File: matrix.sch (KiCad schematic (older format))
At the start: 134 parts, among them SW1 SW_Push, SW10 SW_Push, SW11 SW_Push, SW12 SW_Push, SW13 SW_Push, SW14 SW_Push, SW15 SW_Push, SW16 SW_Push, SW17 SW_Push, SW18 SW_Push, SW19 SW_Push, SW2 SW_Push, SW20 SW_Push, SW21 SW_Push, SW22 SW_Push, SW23 SW_Push, SW24 SW_Push, SW25 SW_Push, SW26 SW_Push, SW27 SW_Push, SW28 SW_Push, SW29 SW_Push, SW3 SW_Push, SW30 SW_Push, SW31 SW_Push, SW32 SW_Push, SW33 SW_Push, SW34 SW_Push, SW35 SW_Push, SW36 SW_Push, SW37 SW_Push, SW38 SW_Push, SW39 SW_Push, SW4 SW_Push, SW40 SW_Push, SW41 SW_Push, SW42 SW_Push, SW43 SW_Push, SW44 SW_Push, SW45 SW_Push, SW46 SW_Push, SW47 SW_Push, SW48 SW_Push, SW49 SW_Push, SW5 SW_Push, SW50 SW_Push, SW51 SW_Push, SW52 SW_Push, SW53 SW_Push, SW54 SW_Push, SW55 SW_Push, SW56 SW_Push, SW57 SW_Push, SW58 SW_Push, SW59 SW_Push, SW6 SW_Push, SW60 SW_Push, SW61 SW_Push, SW62 SW_Push, SW63 SW_Push, SW64 SW_Push, SW65 SW_Push, SW66 SW_Push, SW67 SW_Push, SW7 SW_Push, SW8 SW_Push, SW9 SW_Push

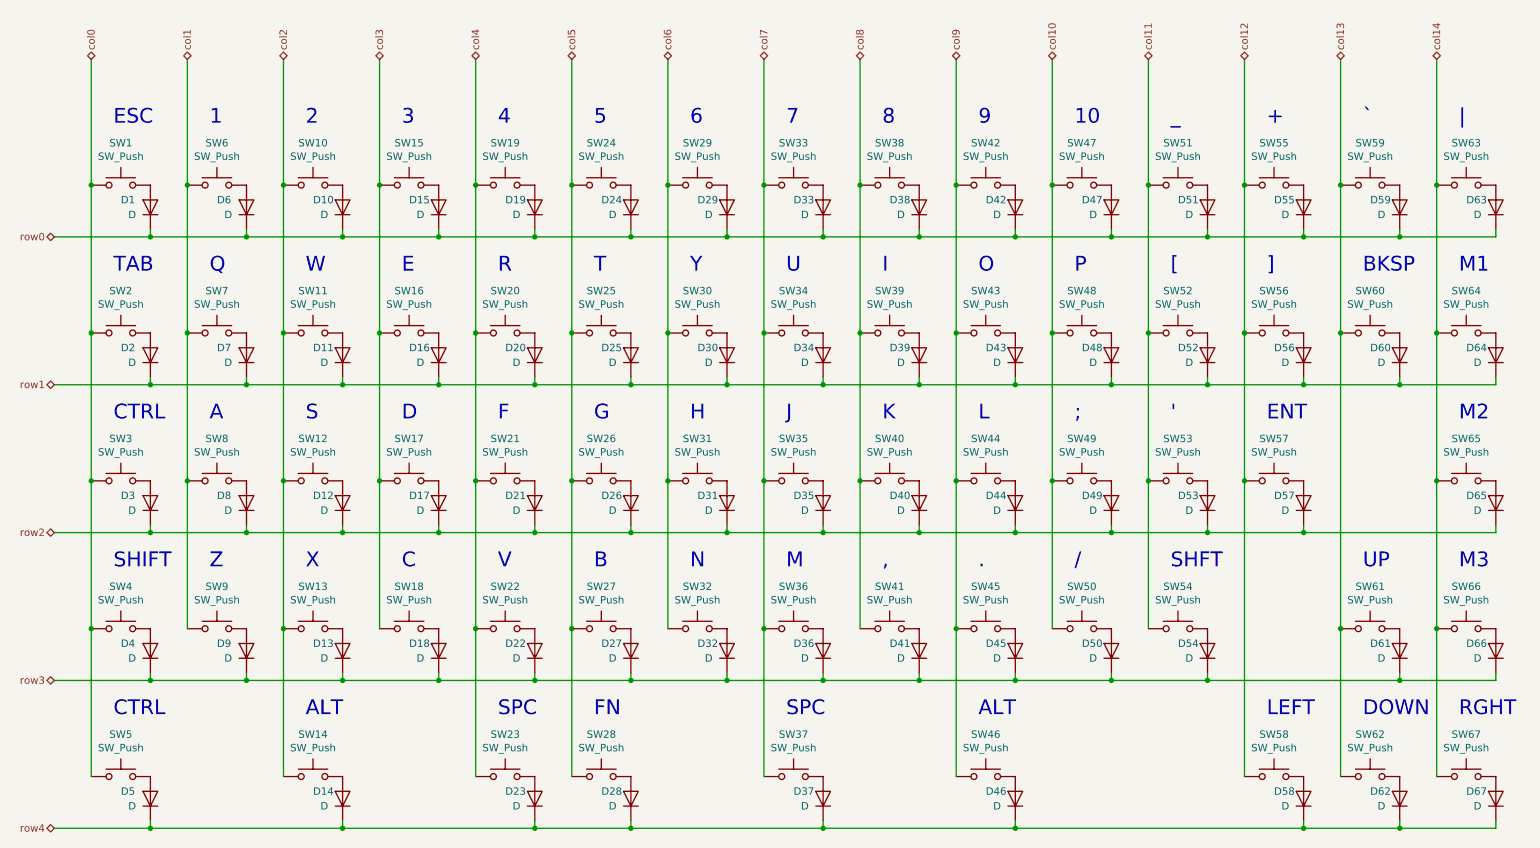
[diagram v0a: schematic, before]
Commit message: Remove top row and decrease all other row indexes by 1 to adjust.
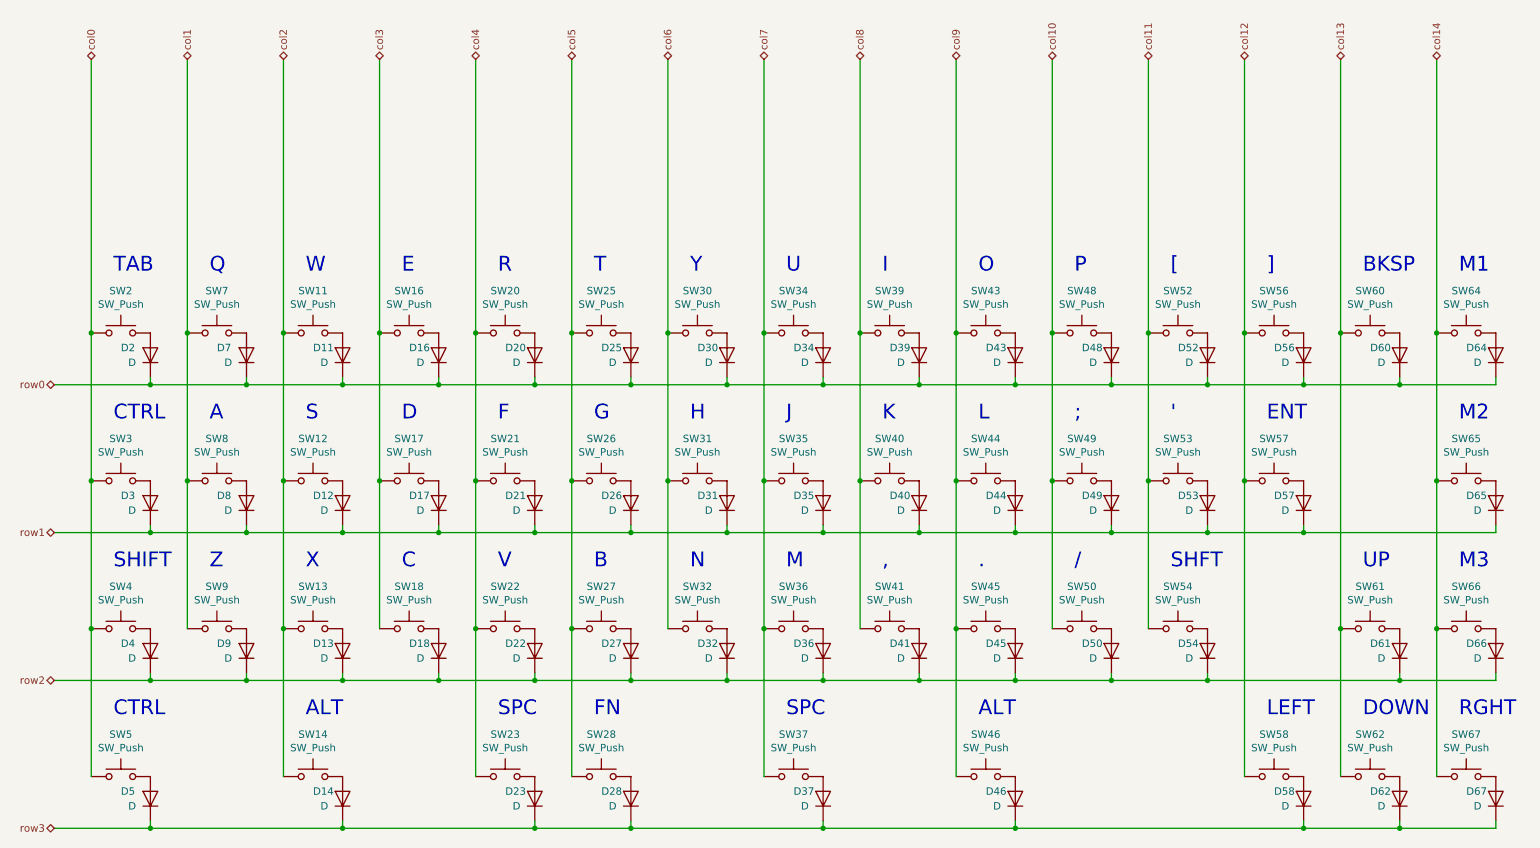
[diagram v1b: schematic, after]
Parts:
- removed D1, D10, D15, D19, D24, D29, D33, D38, D42, D47, D51, D55, D59, D6, D63: D, Diodes_SMD:D_SOD-123, symbol Device:D
- removed SW1, SW10, SW15, SW19, SW24, SW29, SW33, SW38, SW42, SW47, SW51, SW55, SW59, SW6, SW63: SW_Push, Fate_Parts:SW_Cherry_MX_1.00u_PCB, symbol Switch:SW_Push
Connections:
- net row4 is gone; now on net row3: D14.1 (K), D23.1 (K), D28.1 (K), D37.1 (K), D46.1 (K), D5.1 (K), D58.1 (K), D62.1 (K), D67.1 (K)
- net row0: now also D11.1 (K), D16.1 (K), D2.1 (K), D20.1 (K), D25.1 (K), D30.1 (K), D34.1 (K), D39.1 (K), D43.1 (K), D48.1 (K), D52.1 (K), D56.1 (K), D60.1 (K), D64.1 (K), D7.1 (K)
- net row1: now also D12.1 (K), D17.1 (K), D21.1 (K), D26.1 (K), D3.1 (K), D31.1 (K), D35.1 (K), D40.1 (K), D44.1 (K), D49.1 (K), D53.1 (K), D57.1 (K), D65.1 (K), D8.1 (K); no longer D11.1 (K), D16.1 (K), D2.1 (K), D20.1 (K), D25.1 (K), D30.1 (K), D34.1 (K), D39.1 (K), D43.1 (K), D48.1 (K), D52.1 (K), D56.1 (K), D60.1 (K), D64.1 (K), D7.1 (K)
- net row2: now also D13.1 (K), D18.1 (K), D22.1 (K), D27.1 (K), D32.1 (K), D36.1 (K), D4.1 (K), D41.1 (K), D45.1 (K), D50.1 (K), D54.1 (K), D61.1 (K), D66.1 (K), D9.1 (K); no longer D12.1 (K), D17.1 (K), D21.1 (K), D26.1 (K), D3.1 (K), D31.1 (K), D35.1 (K), D40.1 (K), D44.1 (K), D49.1 (K), D53.1 (K), D57.1 (K), D65.1 (K), D8.1 (K)
- net row3: no longer D13.1 (K), D18.1 (K), D22.1 (K), D27.1 (K), D32.1 (K), D36.1 (K), D4.1 (K), D41.1 (K), D45.1 (K), D50.1 (K), D54.1 (K), D61.1 (K), D66.1 (K), D9.1 (K)
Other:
- note removed: "+"
- note removed: "1"
- note removed: "10"
- note removed: "2"
- note removed: "3"
- note removed: "4"
- note removed: "5"
- note removed: "6"
- note removed: "7"
- note removed: "8"
- note removed: "9"
- note removed: "ESC"
- note removed: "_"
- note removed: "`"
- note removed: "|"

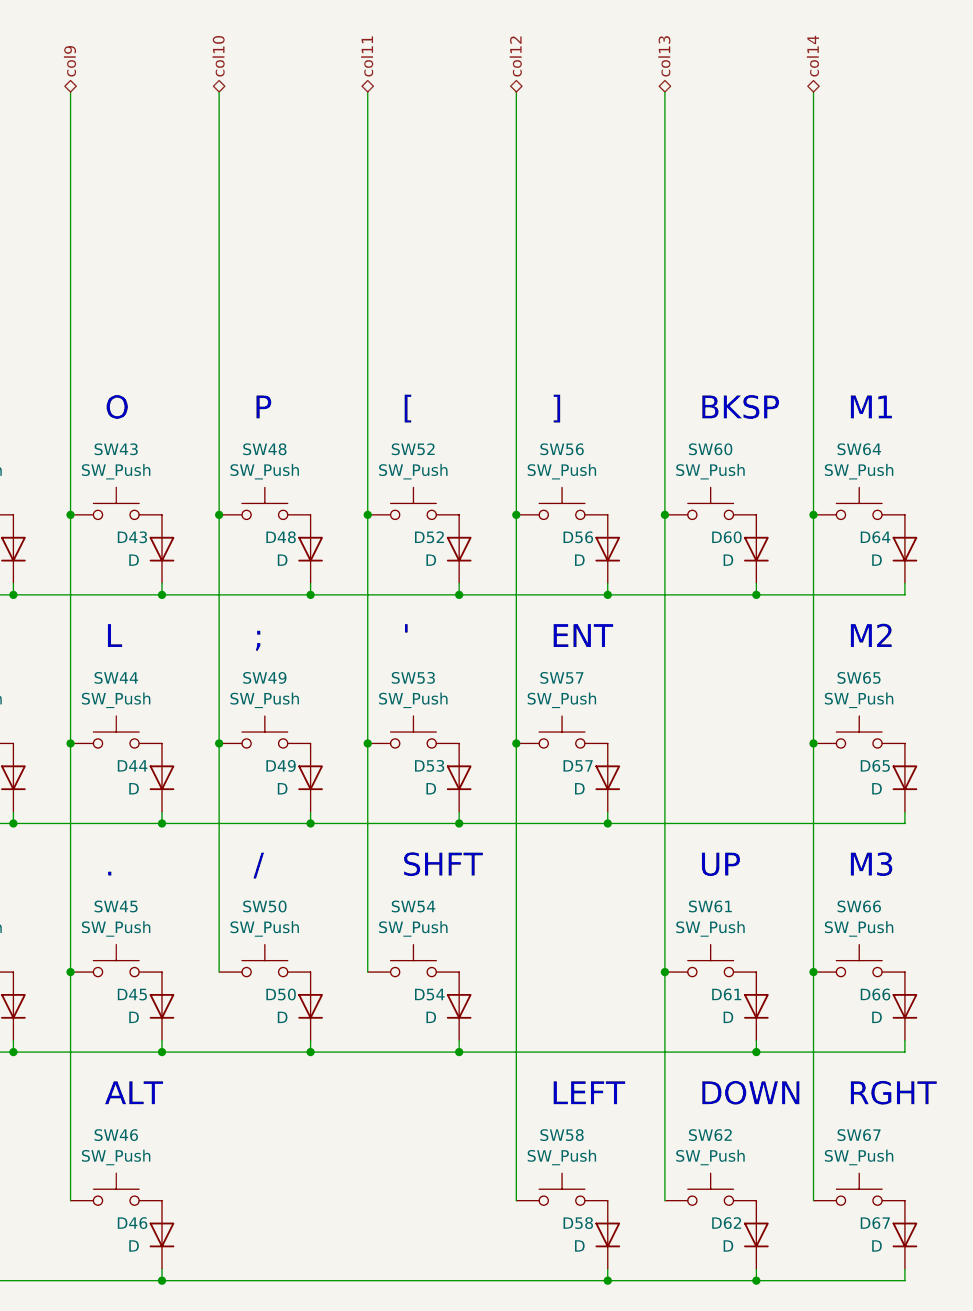
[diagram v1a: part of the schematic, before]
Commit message: Redesign alpha layout for natural finger spread.
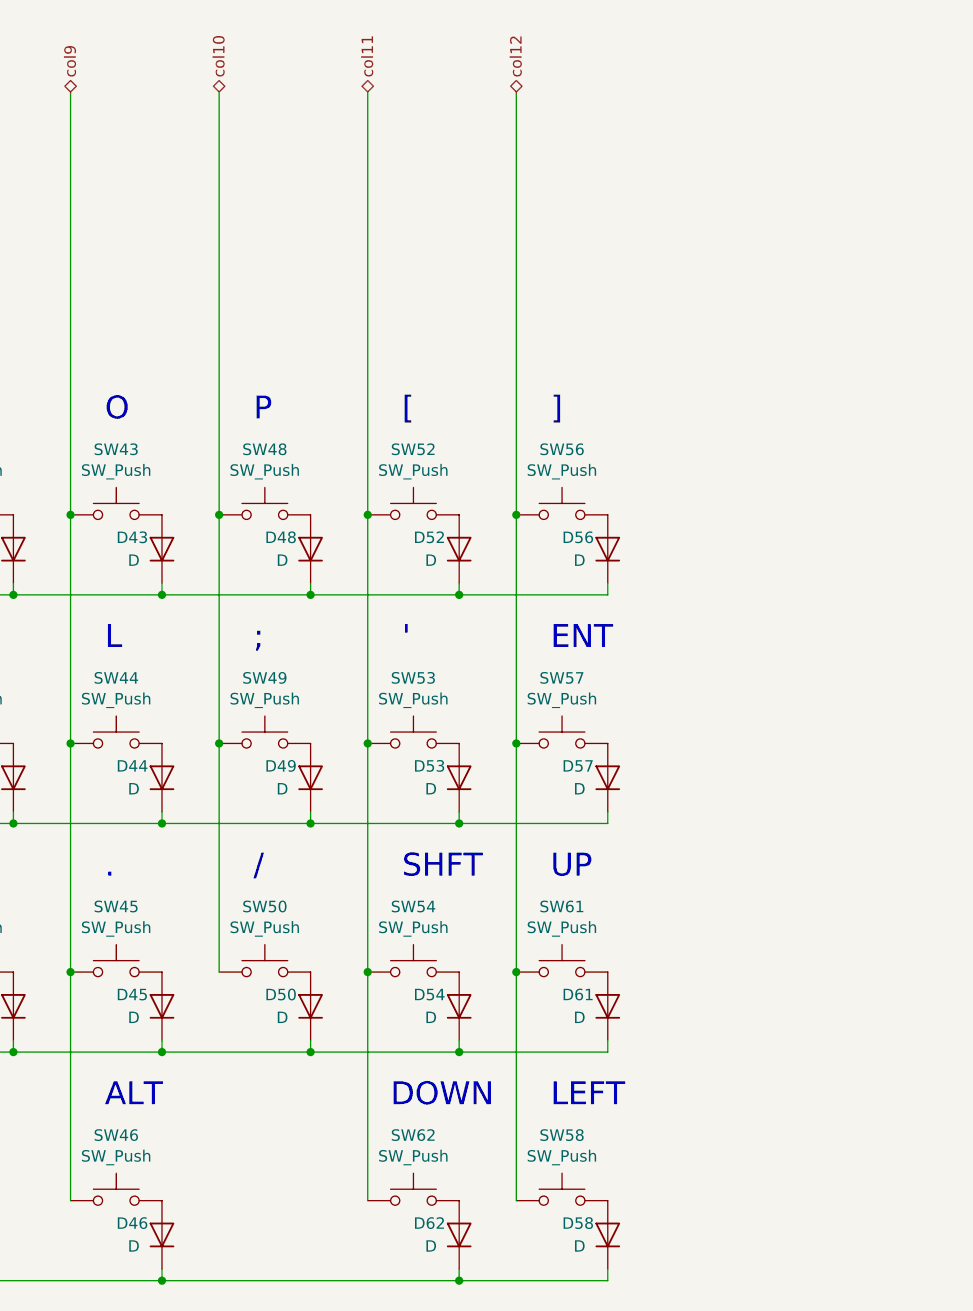
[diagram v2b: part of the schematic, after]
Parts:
- removed D60, D64, D65, D66, D67: D, Diodes_SMD:D_SOD-123, symbol Device:D
- removed SW60: SW_Push, Fate_Parts:SW_Cherry_MX_1.50u_PCB, symbol Switch:SW_Push
- removed SW64, SW65, SW66, SW67: SW_Push, Fate_Parts:SW_Cherry_MX_1.00u_PCB, symbol Switch:SW_Push
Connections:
- net col11: now also SW62.1
- net col12: now also SW61.1
- removed net col13: SW61.1, SW62.1
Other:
- note removed: "BKSP"
- note removed: "M1"
- note removed: "M2"
- note removed: "M3"
- note removed: "RGHT\n"
- moved on the sheet: D61, D62, SW61, SW62
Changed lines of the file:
@@
 Text HLabel 9000 750  1    50   3State ~ 0
 col12
-Text HLabel 9650 750  1    50   3State ~ 0
-col13
-Text HLabel 10300 750  1    50   3State ~ 0
-col14
 Wire Wire Line
 	950  2950 1600 2950
@@
 Connection ~ 9000 2600
 $Comp
-L Switch:SW_Push SW60
-U 1 1 5C6656F5
-P 9850 2600
-F 0 "SW60" H 9850 2885 50  0000 C CNN
-F 1 "SW_Push" H 9850 2794 50  0000 C CNN
-F 2 "Fate_Parts:SW_Cherry_MX_1.50u_PCB" H 9850 2800 50  0001 C CNN
-F 3 "" H 9850 2800 50  0001 C CNN
-	1    9850 2600
-	1    0    0    -1
-$EndComp
-$Comp
-L Device:D D60
-U 1 1 5C6656FC
-P 10050 2750
-F 0 "D60" V 10100 2950 50  0000 R CNN
-F 1 "D" V 10000 2900 50  0000 R CNN
-F 2 "Diodes_SMD:D_SOD-123" H 10050 2750 50  0001 C CNN
-F 3 "~" H 10050 2750 50  0001 C CNN
-	1    10050 2750
-	0    -1   -1   0
-$EndComp
-Wire Wire Line
-	10050 2900 10050 2950
-$Comp
 L Switch:SW_Push SW61
 U 1 1 5C66570E
-P 9850 4600
-F 0 "SW61" H 9850 4885 50  0000 C CNN
-F 1 "SW_Push" H 9850 4794 50  0000 C CNN
-F 2 "Fate_Parts:SW_Cherry_MX_1.00u_PCB" H 9850 4800 50  0001 C CNN
-F 3 "" H 9850 4800 50  0001 C CNN
-	1    9850 4600
-	1    0    0    -1
-$EndComp
-Wire Wire Line
-	9650 4600 9650 5600
+P 9200 4600
+F 0 "SW61" H 9200 4885 50  0000 C CNN
+F 1 "SW_Push" H 9200 4794 50  0000 C CNN
+F 2 "Fate_Parts:SW_Cherry_MX_1.00u_PCB" H 9200 4800 50  0001 C CNN
+F 3 "" H 9200 4800 50  0001 C CNN
+	1    9200 4600
+	1    0    0    -1
+$EndComp
 $Comp
 L Switch:SW_Push SW62
 U 1 1 5C665716
-P 9850 5600
-F 0 "SW62" H 9850 5885 50  0000 C CNN
-F 1 "SW_Push" H 9850 5794 50  0000 C CNN
-F 2 "Fate_Parts:SW_Cherry_MX_1.00u_PCB" H 9850 5800 50  0001 C CNN
-F 3 "" H 9850 5800 50  0001 C CNN
-	1    9850 5600
+P 8550 5600
+F 0 "SW62" H 8550 5885 50  0000 C CNN
+F 1 "SW_Push" H 8550 5794 50  0000 C CNN
+F 2 "Fate_Parts:SW_Cherry_MX_1.00u_PCB" H 8550 5800 50  0001 C CNN
+F 3 "" H 8550 5800 50  0001 C CNN
+	1    8550 5600
 	1    0    0    -1
 $EndComp
@@
 L Device:D D61
 U 1 1 5C665724
-P 10050 4750
-F 0 "D61" V 10100 4950 50  0000 R CNN
-F 1 "D" V 10000 4900 50  0000 R CNN
-F 2 "Diodes_SMD:D_SOD-123" H 10050 4750 50  0001 C CNN
-F 3 "~" H 10050 4750 50  0001 C CNN
-	1    10050 4750
+P 9400 4750
+F 0 "D61" V 9450 4950 50  0000 R CNN
+F 1 "D" V 9350 4900 50  0000 R CNN
+F 2 "Diodes_SMD:D_SOD-123" H 9400 4750 50  0001 C CNN
+F 3 "~" H 9400 4750 50  0001 C CNN
+	1    9400 4750
 	0    -1   -1   0
 $EndComp
@@
 L Device:D D62
 U 1 1 5C66572B
-P 10050 5750
-F 0 "D62" V 10100 5950 50  0000 R CNN
-F 1 "D" V 10000 5900 50  0000 R CNN
-F 2 "Diodes_SMD:D_SOD-123" H 10050 5750 50  0001 C CNN
-F 3 "~" H 10050 5750 50  0001 C CNN
-	1    10050 5750
-	0    -1   -1   0
-$EndComp
-Wire Wire Line
-	10050 5900 10050 5950
-Wire Wire Line
-	10050 4900 10050 4950
-Connection ~ 9650 4600
-Connection ~ 9650 2600
-$Comp
-L Switch:SW_Push SW64
-U 1 1 5C66EC7D
-P 10500 2600
-F 0 "SW64" H 10500 2885 50  0000 C CNN
-F 1 "SW_Push" H 10500 2794 50  0000 C CNN
-F 2 "Fate_Parts:SW_Cherry_MX_1.00u_PCB" H 10500 2800 50  0001 C CNN
-F 3 "" H 10500 2800 50  0001 C CNN
-	1    10500 2600
-	1    0    0    -1
-$EndComp
-$Comp
-L Device:D D64
-U 1 1 5C66EC84
-P 10700 2750
-F 0 "D64" V 10750 2950 50  0000 R CNN
-F 1 "D" V 10650 2900 50  0000 R CNN
-F 2 "Diodes_SMD:D_SOD-123" H 10700 2750 50  0001 C CNN
-F 3 "~" H 10700 2750 50  0001 C CNN
-	1    10700 2750
-	0    -1   -1   0
-$EndComp
-Wire Wire Line
-	10700 2900 10700 2950
-$Comp
-L Switch:SW_Push SW65
-U 1 1 5C66EC8F
-P 10500 3600
-F 0 "SW65" H 10500 3885 50  0000 C CNN
-F 1 "SW_Push" H 10500 3794 50  0000 C CNN
-F 2 "Fate_Parts:SW_Cherry_MX_1.00u_PCB" H 10500 3800 50  0001 C CNN
-F 3 "" H 10500 3800 50  0001 C CNN
-	1    10500 3600
-	1    0    0    -1
-$EndComp
-$Comp
-L Switch:SW_Push SW66
-U 1 1 5C66EC96
-P 10500 4600
-F 0 "SW66" H 10500 4885 50  0000 C CNN
-F 1 "SW_Push" H 10500 4794 50  0000 C CNN
-F 2 "Fate_Parts:SW_Cherry_MX_1.00u_PCB" H 10500 4800 50  0001 C CNN
-F 3 "" H 10500 4800 50  0001 C CNN
-	1    10500 4600
-	1    0    0    -1
-$EndComp
-Wire Wire Line
-	10300 4600 10300 5600
-$Comp
-L Switch:SW_Push SW67
-U 1 1 5C66EC9E
-P 10500 5600
-F 0 "SW67" H 10500 5885 50  0000 C CNN
-F 1 "SW_Push" H 10500 5794 50  0000 C CNN
-F 2 "Fate_Parts:SW_Cherry_MX_1.00u_PCB" H 10500 5800 50  0001 C CNN
-F 3 "" H 10500 5800 50  0001 C CNN
-	1    10500 5600
-	1    0    0    -1
-$EndComp
-$Comp
-L Device:D D65
-U 1 1 5C66ECA5
-P 10700 3750
-F 0 "D65" V 10750 3950 50  0000 R CNN
-F 1 "D" V 10650 3900 50  0000 R CNN
-F 2 "Diodes_SMD:D_SOD-123" H 10700 3750 50  0001 C CNN
-F 3 "~" H 10700 3750 50  0001 C CNN
-	1    10700 3750
-	0    -1   -1   0
-$EndComp
-$Comp
-L Device:D D66
-U 1 1 5C66ECAC
-P 10700 4750
-F 0 "D66" V 10750 4950 50  0000 R CNN
-F 1 "D" V 10650 4900 50  0000 R CNN
-F 2 "Diodes_SMD:D_SOD-123" H 10700 4750 50  0001 C CNN
-F 3 "~" H 10700 4750 50  0001 C CNN
-	1    10700 4750
-	0    -1   -1   0
-$EndComp
-$Comp
-L Device:D D67
-U 1 1 5C66ECB3
-P 10700 5750
-F 0 "D67" V 10750 5950 50  0000 R CNN
-F 1 "D" V 10650 5900 50  0000 R CNN
-F 2 "Diodes_SMD:D_SOD-123" H 10700 5750 50  0001 C CNN
-F 3 "~" H 10700 5750 50  0001 C CNN
-	1    10700 5750
-	0    -1   -1   0
-$EndComp
-Wire Wire Line
-	10700 5900 10700 5950
-Wire Wire Line
-	10700 4900 10700 4950
-Wire Wire Line
-	10700 3900 10700 3950
-Connection ~ 10300 4600
-Wire Wire Line
-	10300 3600 10300 4600
-Connection ~ 10300 2600
+P 8750 5750
+F 0 "D62" V 8800 5950 50  0000 R CNN
+F 1 "D" V 8700 5900 50  0000 R CNN
+F 2 "Diodes_SMD:D_SOD-123" H 8750 5750 50  0001 C CNN
+F 3 "~" H 8750 5750 50  0001 C CNN
+	1    8750 5750
+	0    -1   -1   0
+$EndComp
 Text Notes 1350 2200 0    100  ~ 0
 TAB
@@
 Text Notes 9150 2200 0    100  ~ 0
 ]
-Text Notes 9800 2200 0    100  ~ 0
-BKSP
-Text Notes 10450 2200 0    100  ~ 0
-M1
 Text Notes 1350 3200 0    100  ~ 0
 CTRL
@@
 Wire Wire Line
 	8750 2950 9400 2950
-Connection ~ 9400 2950
-Wire Wire Line
-	9400 2950 10050 2950
-Connection ~ 10050 2950
-Wire Wire Line
-	10050 2950 10700 2950
 Wire Wire Line
 	2250 3950 2900 3950
@@
 Wire Wire Line
 	8750 3950 9400 3950
-Connection ~ 9400 3950
 Connection ~ 1600 4950
 Wire Wire Line
@@
 	8100 4950 8750 4950
 Connection ~ 8750 4950
-Connection ~ 10050 4950
-Wire Wire Line
-	10050 4950 10700 4950
 Connection ~ 2900 5950
 Connection ~ 4200 5950
@@
 Connection ~ 6150 5950
 Connection ~ 7450 5950
-Connection ~ 9400 5950
-Wire Wire Line
-	9400 5950 10050 5950
-Connection ~ 10050 5950
-Wire Wire Line
-	10050 5950 10700 5950
 Text Notes 2000 3200 0    100  ~ 0
 A
@@
 Wire Wire Line
 	9000 2600 9000 3600
-Connection ~ 10300 3600
-Wire Wire Line
-	10300 2600 10300 3600
 Text Notes 2650 3200 0    100  ~ 0
 S
@@
 Text Notes 8500 4200 0    100  ~ 0
 SHFT
-Text Notes 9800 4200 0    100  ~ 0
-UP
 Text Notes 1350 5200 0    100  ~ 0
 CTRL
@@
 Text Notes 5900 5200 0    100  ~ 0
 SPC
-Text Notes 9800 5200 0    100  ~ 0
+Text Notes 8450 5200 0    100  ~ 0
 DOWN
 Text Notes 9150 5200 0    100  ~ 0
 LEFT
-Text Notes 10450 5200 0    100  ~ 0
-RGHT\n
-Text Notes 10450 3200 0    100  ~ 0
-M2
-Text Notes 10450 4200 0    100  ~ 0
-M3
-Wire Wire Line
-	9650 2600 9650 4600
-Wire Wire Line
-	9400 3950 10700 3950
-Wire Wire Line
-	9000 3600 9000 5600
-Wire Wire Line
-	8750 4950 10050 4950
-Wire Wire Line
-	7450 5950 9400 5950
+Wire Wire Line
+	9000 3600 9000 4600
+Wire Wire Line
+	8750 4950 9400 4950
+Wire Wire Line
+	7450 5950 8750 5950
 Wire Wire Line
 	6150 5950 7450 5950
@@
 Wire Wire Line
 	9000 750  9000 2600
-Wire Wire Line
-	9650 750  9650 2600
-Wire Wire Line
-	10300 750  10300 2600
 Text HLabel 1200 750  1    50   3State ~ 0
 col0
+Text Notes 9150 4200 0    100  ~ 0
+UP
+Connection ~ 9000 4600
+Wire Wire Line
+	9000 4600 9000 5600
+Wire Wire Line
+	9400 4900 9400 4950
+Wire Wire Line
+	8350 4600 8350 5600
+Connection ~ 8350 4600
+Wire Wire Line
+	8750 5900 8750 5950
+Connection ~ 8750 5950
+Wire Wire Line
+	8750 5950 9400 5950
 $EndSCHEMATC
